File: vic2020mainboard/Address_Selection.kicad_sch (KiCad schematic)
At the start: 19 parts, among them SW1 RAM ENABLE, U1 7402, U10 74LS133, U11 74LS02, U2 74LS138, U24 74ALS32, U4 7406, U5 74LS133, U6 74LS138, U8 74LS00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

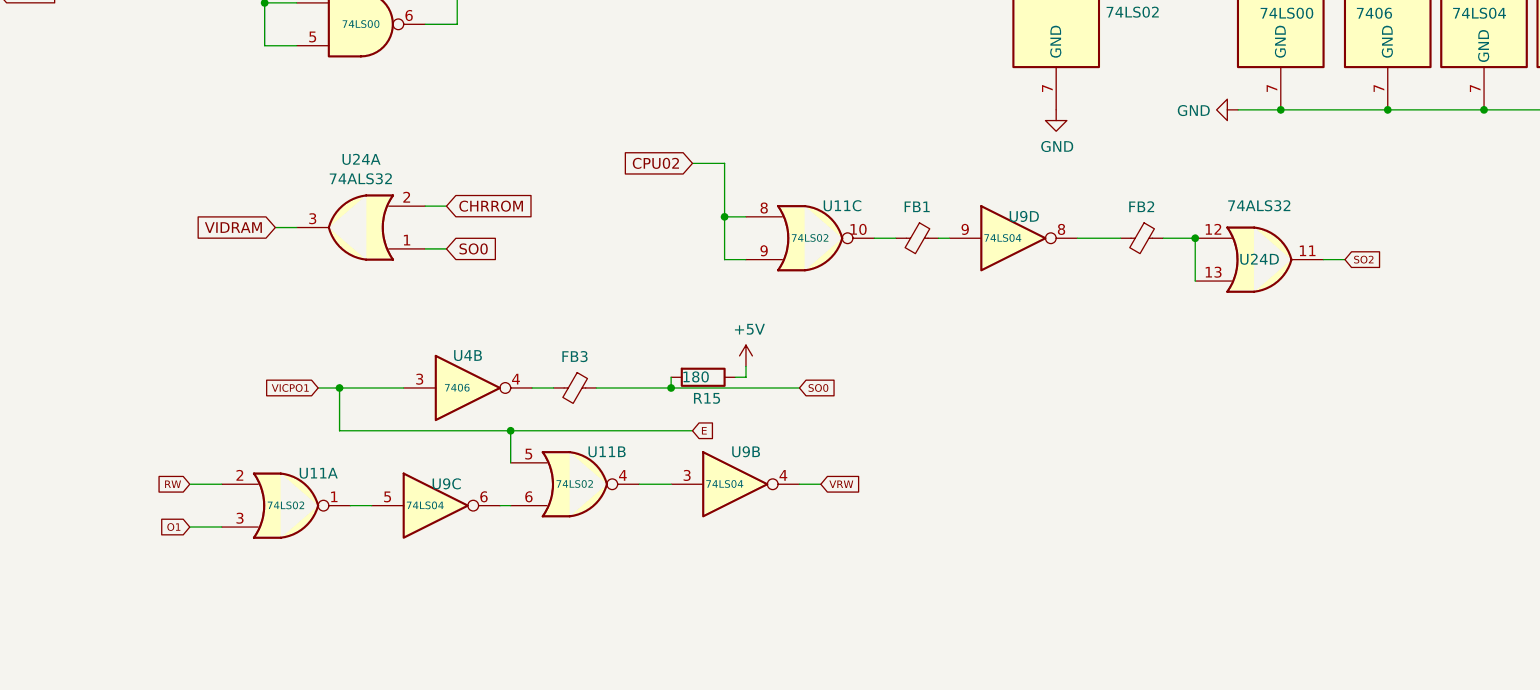
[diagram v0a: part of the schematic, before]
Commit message: Added power supply circuit for 9V AC input
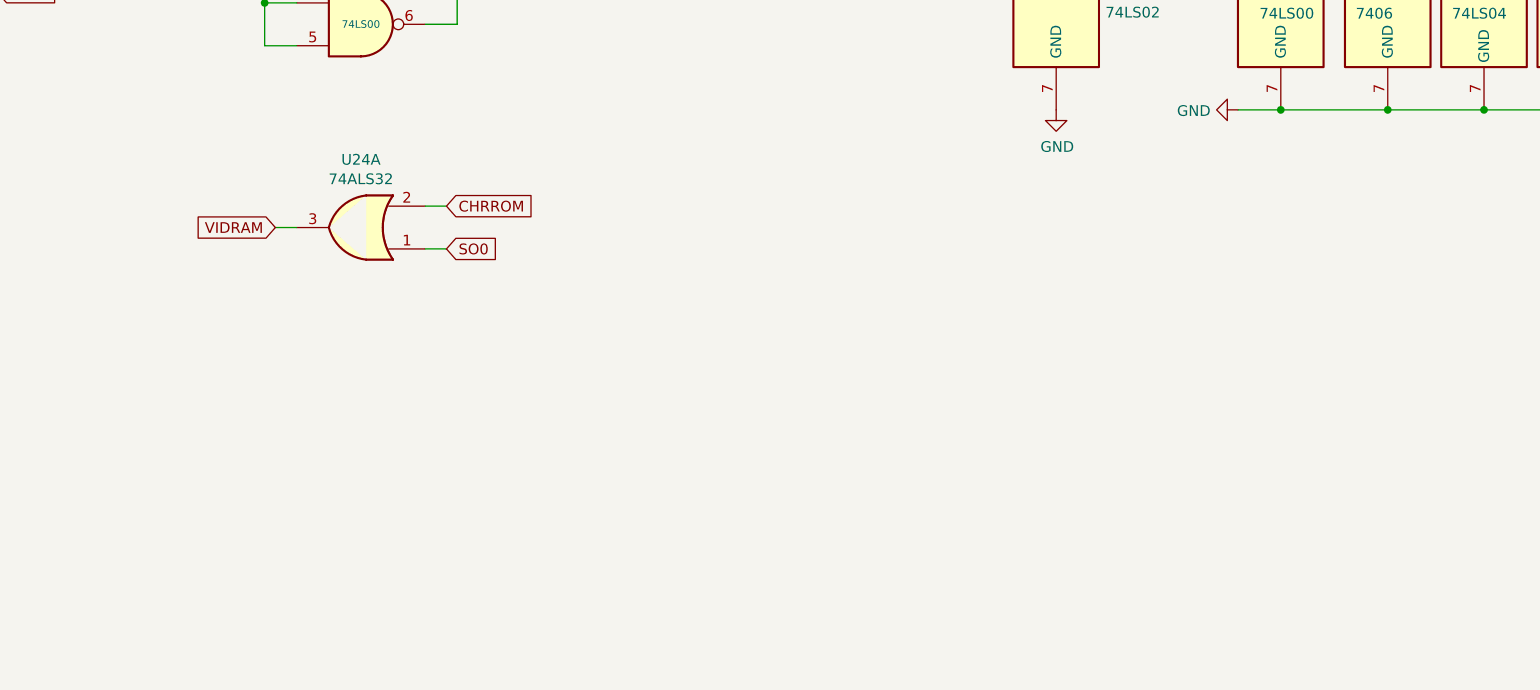
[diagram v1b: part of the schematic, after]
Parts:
- removed FB1, FB2, FB3: Ferrite_Bead_Small, Inductor_THT:L_Axial_L6.6mm_D2.7mm_P10.16mm_Horizontal_Vishay_IM-2, symbol Vic2020mainboard-rescue:Ferrite_Bead_Small-Device
- removed R15: 180, Resistor_THT:R_Axial_DIN0207_L6.3mm_D2.5mm_P7.62mm_Horizontal, symbol Device:R
- removed unit 1 of U11
- removed unit 2 of U11
- removed unit 3 of U11
- removed unit 4 of U24
- removed unit 2 of U4
- removed unit 2 of U9
- removed unit 4 of U9
- removed unit 3 of U9
